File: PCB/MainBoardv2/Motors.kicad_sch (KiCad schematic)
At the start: 12 parts, among them J21 Screw_Terminal_01x02, J22 Screw_Terminal_01x02, J23 Screw_Terminal_01x02

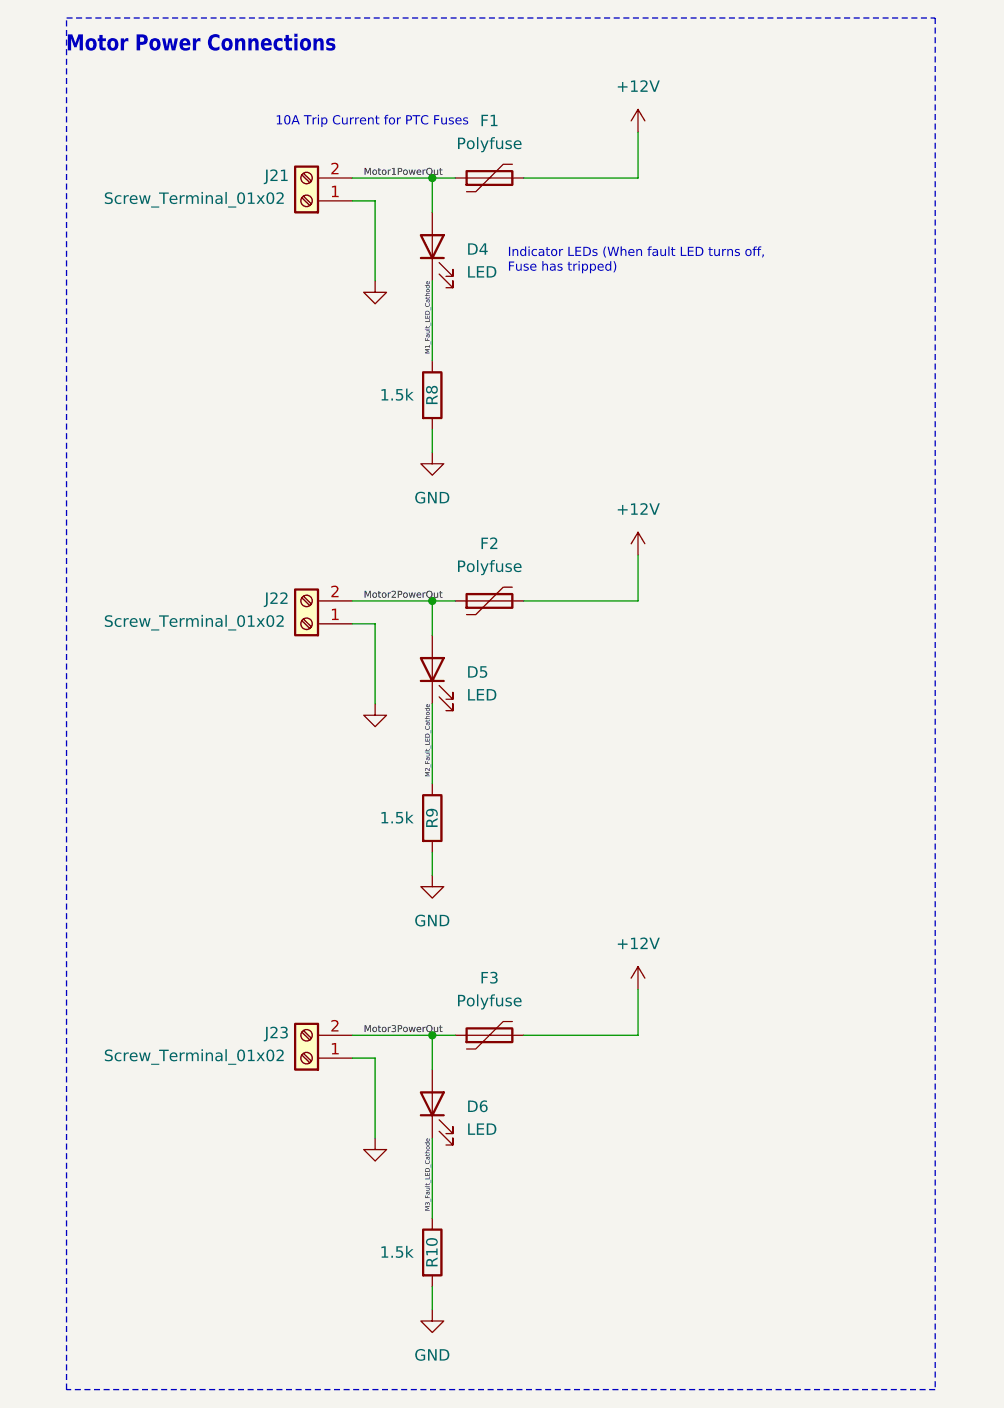
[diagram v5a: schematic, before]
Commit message: updating layout progress, adding limit switch extra circuitry
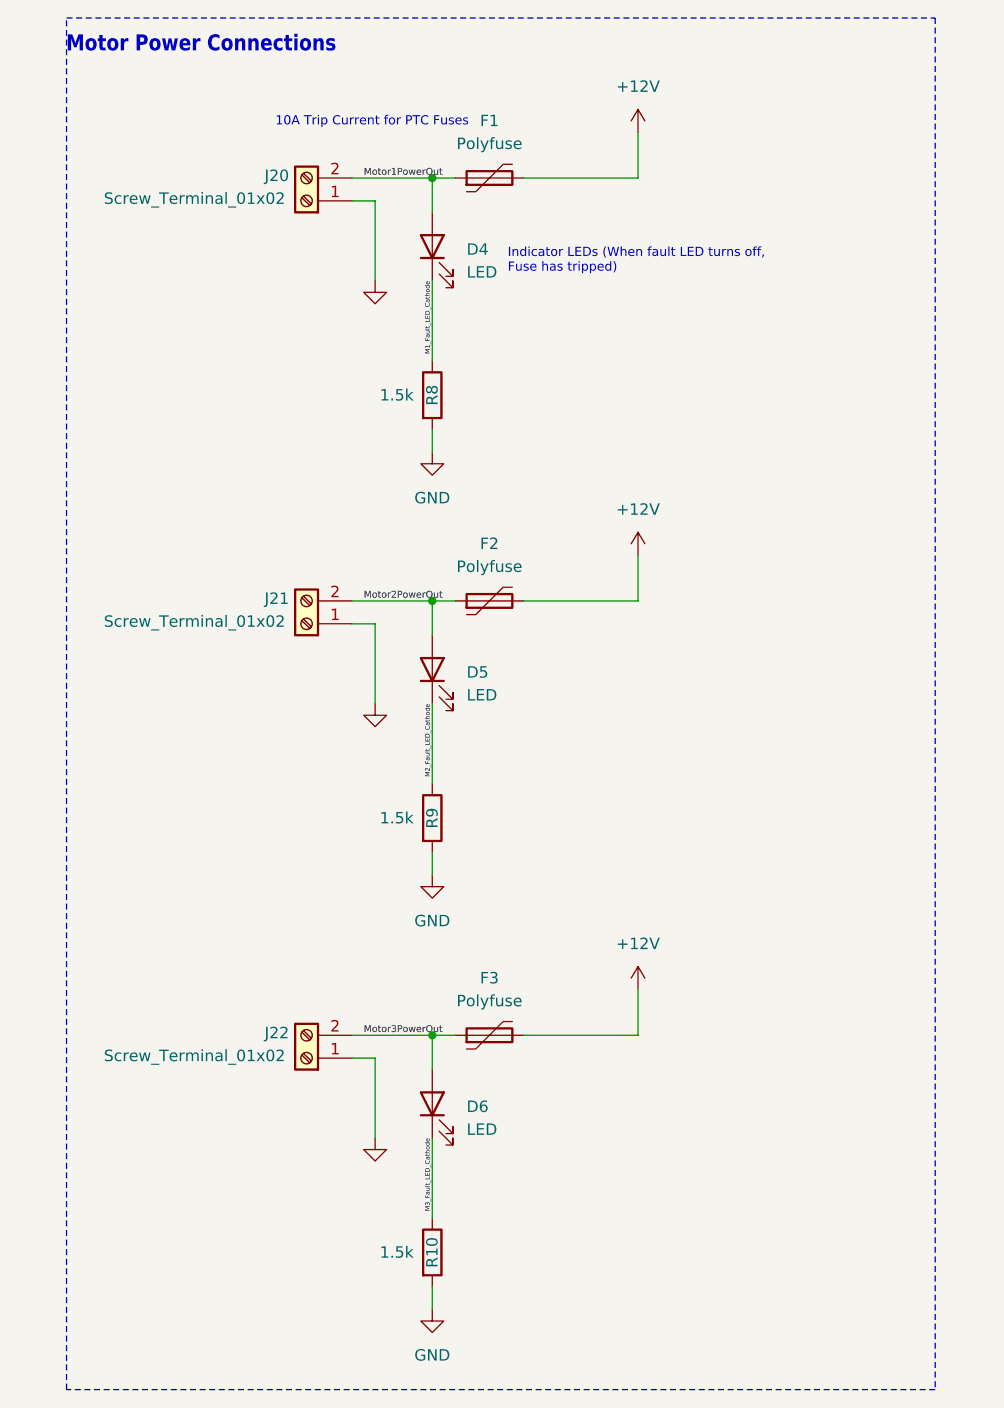
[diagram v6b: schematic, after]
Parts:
- renumbered J21 to J20, J22 to J21, J23 to J22
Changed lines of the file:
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@@
 		(dnp no)
 		(fields_autoplaced yes)
-		(property "Reference" "#PWR048"
+		(property "Reference" "#PWR044"
 			(at 101.6 90.17 0)
 			(effects
@@
 			(project "MainBoardv2"
 				(path "/d9c43b87-8960-41bd-bfcc-9c305bab2f72/0b6d272a-beab-45a0-995b-a46a98d72224"
-					(reference "#PWR048")
+					(reference "#PWR044")
 					(unit 1)
 				)
@@
 		(dnp no)
 		(fields_autoplaced yes)
-		(property "Reference" "#PWR047"
+		(property "Reference" "#PWR043"
 			(at 78.74 81.28 0)
 			(effects
@@
 			(project "MainBoardv2"
 				(path "/d9c43b87-8960-41bd-bfcc-9c305bab2f72/0b6d272a-beab-45a0-995b-a46a98d72224"
-					(reference "#PWR047")
+					(reference "#PWR043")
 					(unit 1)
 				)
@@
 		(dnp no)
 		(fields_autoplaced yes)
-		(property "Reference" "#PWR046"
+		(property "Reference" "#PWR042"
 			(at 72.39 62.23 0)
 			(effects
@@
 			(project "MainBoardv2"
 				(path "/d9c43b87-8960-41bd-bfcc-9c305bab2f72/0b6d272a-beab-45a0-995b-a46a98d72224"
-					(reference "#PWR046")
+					(reference "#PWR042")
 					(unit 1)
 				)
@@
 		(on_board yes)
 		(dnp no)
-		(property "Reference" "J23"
+		(property "Reference" "J22"
 			(at 61.468 139.446 0)
 			(effects
@@
 			(project "MainBoardv2"
 				(path "/d9c43b87-8960-41bd-bfcc-9c305bab2f72/0b6d272a-beab-45a0-995b-a46a98d72224"
-					(reference "J23")
+					(reference "J22")
 					(unit 1)
 				)
@@
 		(dnp no)
 		(fields_autoplaced yes)
-		(property "Reference" "#PWR053"
+		(property "Reference" "#PWR049"
 			(at 78.74 176.53 0)
 			(effects
@@
 			(project "MainBoardv2"
 				(path "/d9c43b87-8960-41bd-bfcc-9c305bab2f72/0b6d272a-beab-45a0-995b-a46a98d72224"
-					(reference "#PWR053")
+					(reference "#PWR049")
 					(unit 1)
 				)
@@
 		(on_board yes)
 		(dnp no)
-		(property "Reference" "J21"
+		(property "Reference" "J20"
 			(at 61.468 44.196 0)
 			(effects
@@
 			(project "MainBoardv2"
 				(path "/d9c43b87-8960-41bd-bfcc-9c305bab2f72/0b6d272a-beab-45a0-995b-a46a98d72224"
-					(reference "J21")
+					(reference "J20")
 					(unit 1)
 				)
@@
 		(dnp no)
 		(fields_autoplaced yes)
-		(property "Reference" "#PWR050"
+		(property "Reference" "#PWR046"
 			(at 78.74 128.27 0)
 			(effects
@@
 			(project "MainBoardv2"
 				(path "/d9c43b87-8960-41bd-bfcc-9c305bab2f72/0b6d272a-beab-45a0-995b-a46a98d72224"
-					(reference "#PWR050")
+					(reference "#PWR046")
 					(unit 1)
 				)
@@
 		(on_board yes)
 		(dnp no)
-		(property "Reference" "J22"
+		(property "Reference" "J21"
 			(at 61.468 91.186 0)
 			(effects
@@
 			(project "MainBoardv2"
 				(path "/d9c43b87-8960-41bd-bfcc-9c305bab2f72/0b6d272a-beab-45a0-995b-a46a98d72224"
-					(reference "J22")
+					(reference "J21")
 					(unit 1)
 				)
@@
 		(dnp no)
 		(fields_autoplaced yes)
-		(property "Reference" "#PWR051"
+		(property "Reference" "#PWR047"
 			(at 101.6 138.43 0)
 			(effects
@@
 			(project "MainBoardv2"
 				(path "/d9c43b87-8960-41bd-bfcc-9c305bab2f72/0b6d272a-beab-45a0-995b-a46a98d72224"
-					(reference "#PWR051")
+					(reference "#PWR047")
 					(unit 1)
 				)
@@
 		(dnp no)
 		(fields_autoplaced yes)
-		(property "Reference" "#PWR049"
+		(property "Reference" "#PWR045"
 			(at 72.39 109.22 0)
 			(effects
@@
 			(project "MainBoardv2"
 				(path "/d9c43b87-8960-41bd-bfcc-9c305bab2f72/0b6d272a-beab-45a0-995b-a46a98d72224"
-					(reference "#PWR049")
+					(reference "#PWR045")
 					(unit 1)
 				)
@@
 		(dnp no)
 		(fields_autoplaced yes)
-		(property "Reference" "#PWR052"
+		(property "Reference" "#PWR048"
 			(at 72.39 157.48 0)
 			(effects
@@
 			(project "MainBoardv2"
 				(path "/d9c43b87-8960-41bd-bfcc-9c305bab2f72/0b6d272a-beab-45a0-995b-a46a98d72224"
-					(reference "#PWR052")
+					(reference "#PWR048")
 					(unit 1)
 				)
@@
 		(dnp no)
 		(fields_autoplaced yes)
-		(property "Reference" "#PWR045"
+		(property "Reference" "#PWR041"
 			(at 101.6 43.18 0)
 			(effects
@@
 			(project "MainBoardv2"
 				(path "/d9c43b87-8960-41bd-bfcc-9c305bab2f72/0b6d272a-beab-45a0-995b-a46a98d72224"
-					(reference "#PWR045")
-					(unit 1)
-				)
+					(reference "#PWR041")
+					(unit 1)
+				)
